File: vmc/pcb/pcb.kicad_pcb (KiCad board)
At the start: 2 copper layers, 85 x 90 mm, 88 parts, among them J1 Conn_02x08_Odd_Even, J10 ONE_WIRE_1, J11 ONE_WIRE_2, J12 AUX_1, J13 AUX_2, J14 AUX_3, J2 Conn_01x02_Pin, J3 24VAC, J4 MDB_CONN, J5 I2C header, J6 24VDC, J7 Conn_01x02, J8 Conn_01x02, J9 PICO_DEBUG_HEADER, Q1 BSS138, Q10 BSS138, Q11 BSS138, Q12 BSS138, Q13 BSS138, Q14 BC817, Q15 MMBT3906, Q16 BSS138, Q17 MMBT3906, Q2 BSS138, Q3 BSS138, Q4 BSS138, Q5 BSS138, Q6 BSS138, Q7 BSS138, Q8 BSS138, Q9 BSS138, U1 Pico, U2 74LS14

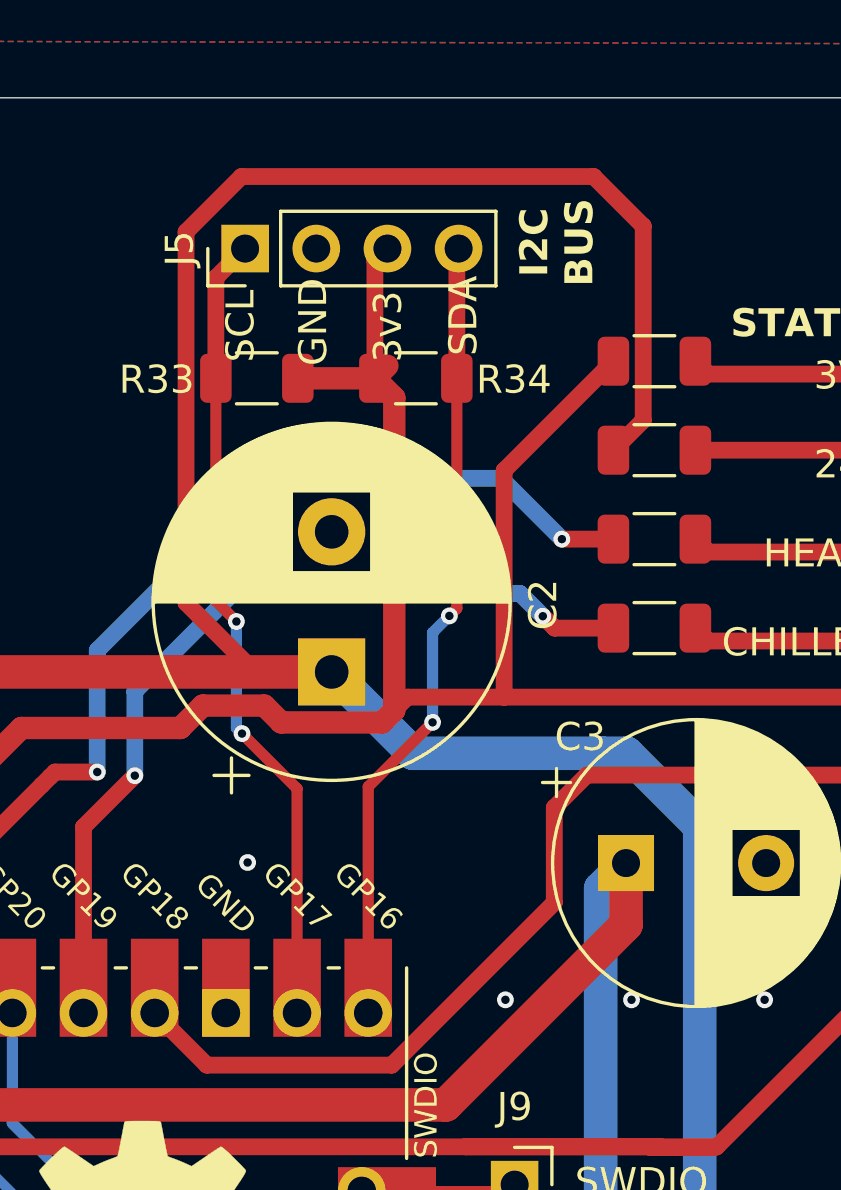
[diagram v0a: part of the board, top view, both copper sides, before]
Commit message: Updated PCB to thicken i2c data tracks and reroute the 24v led feed
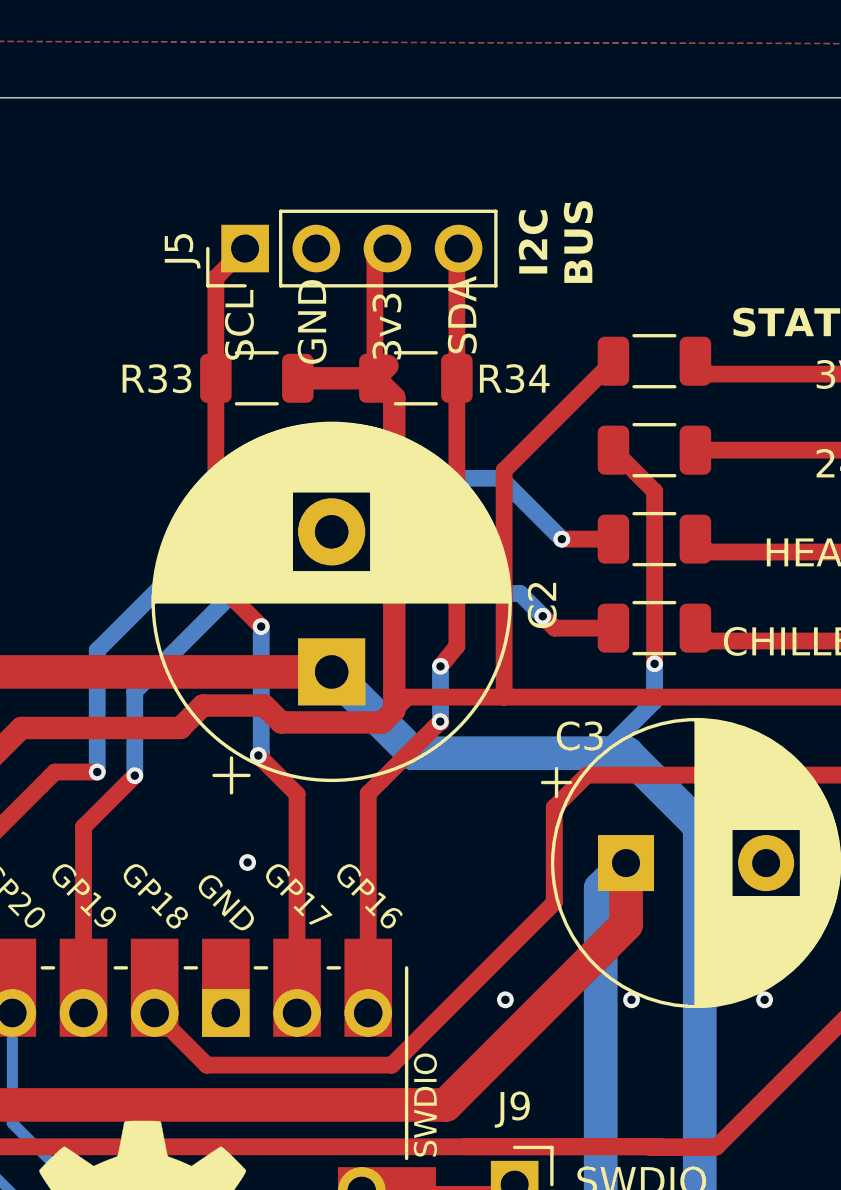
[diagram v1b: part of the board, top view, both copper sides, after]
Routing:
- net +24V: track 160.6 -> 127.0 mm, vias 0 -> 1
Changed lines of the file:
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@@
-	)
-	(segment
-		(start 60.773481 18)
-		(end 73.346502 18)
-		(width 0.6)
-		(layer "F.Cu")
-		(net 34)
-	)
-	(segment
-		(start 75.1135 19.766998)
-		(end 75.1135 26.7015)
-		(width 0.6)
-		(layer "F.Cu")
-		(net 34)
 	)
 	(segment
@@
 	)
 	(segment
-		(start 63.995481 35.678787)
-		(end 61.262695 35.678787)
-		(width 0.6)
-		(layer "F.Cu")
-		(net 34)
-	)
-	(segment
 		(start 46.878787 35.678787)
 		(end 46.84 35.64)
@@
 	)
 	(segment
-		(start 58.799 19.974481)
-		(end 60.773481 18)
+		(start 75.52 29.235)
+		(end 75.52 35.39)
 		(width 0.6)
 		(layer "F.Cu")
@@
 	)
 	(segment
-		(start 73.346502 18)
-		(end 75.1135 19.766998)
-		(width 0.6)
-		(layer "F.Cu")
-		(net 34)
-	)
-	(segment
-		(start 58.799 33.215092)
-		(end 58.799 19.974481)
-		(width 0.6)
-		(layer "F.Cu")
-		(net 34)
-	)
-	(segment
 		(start 63.935481 35.618787)
 		(end 63.995481 35.678787)
@@
 	)
 	(segment
-		(start 75.1135 26.7015)
-		(end 74.05 27.765)
-		(width 0.6)
-		(layer "F.Cu")
-		(net 34)
-	)
-	(segment
-		(start 61.262695 35.678787)
-		(end 58.799 33.215092)
+		(start 74.05 27.765)
+		(end 75.52 29.235)
 		(width 0.6)
 		(layer "F.Cu")
@@
 		(net 34)
 	)
+	(via
+		(at 75.52 35.39)
+		(size 0.6)
+		(drill 0.3)
+		(layers "F.Cu" "B.Cu")
+		(net 34)
+	)
 	(segment
 		(start 81.901531 74.651531)
@@
 	)
 	(segment
+		(start 75.52 36.719787)
+		(end 73.66 38.579787)
+		(width 0.6)
+		(layer "B.Cu")
+		(net 34)
+	)
+	(segment
 		(start 73.66 38.579787)
 		(end 66.896481 38.579787)
@@
 	)
 	(segment
+		(start 75.52 35.39)
+		(end 75.52 36.719787)
+		(width 0.6)
+		(layer "B.Cu")
+		(net 34)
+	)
+	(segment
 		(start 81.901531 90.157611)
 		(end 81.901531 74.651531)
@@
 	)
 	(segment
-		(start 60.595481 33.878787)
-		(end 59.8625 33.145806)
-		(width 0.4)
+		(start 62.76 40.04)
+		(end 61.38 38.66)
+		(width 0.6)
 		(layer "F.Cu")
 		(net 48)
@@
 	)
 	(segment
-		(start 59.8625 33.145806)
-		(end 59.8625 25.2)
-		(width 0.4)
-		(layer "F.Cu")
-		(net 48)
-	)
-	(segment
-		(start 62.76 39.843306)
-		(end 60.795481 37.878787)
-		(width 0.4)
+		(start 59.8625 25.2)
+		(end 59.8625 32.4425)
+		(width 0.6)
+		(layer "F.Cu")
+		(net 48)
+	)
+	(segment
+		(start 59.8625 32.4425)
+		(end 61.48 34.06)
+		(width 0.6)
 		(layer "F.Cu")
 		(net 48)
@@
 	(segment
 		(start 62.76 47.848787)
-		(end 62.76 39.843306)
-		(width 0.4)
+		(end 62.76 40.04)
+		(width 0.6)
 		(layer "F.Cu")
 		(net 48)
@@
 	)
 	(via
-		(at 60.595481 33.878787)
-		(size 0.6)
-		(drill 0.3)
-		(layers "F.Cu" "B.Cu")
-		(net 48)
-	)
-	(via
-		(at 60.795481 37.878787)
-		(size 0.6)
-		(drill 0.3)
-		(layers "F.Cu" "B.Cu")
-		(net 48)
-	)
-	(segment
-		(start 60.595481 33.878787)
-		(end 60.595481 37.678787)
-		(width 0.4)
-		(layer "B.Cu")
-		(net 48)
-	)
-	(segment
-		(start 60.595481 37.678787)
-		(end 60.795481 37.878787)
-		(width 0.4)
-		(layer "B.Cu")
-		(net 48)
-	)
-	(segment
-		(start 65.3 39.774268)
-		(end 67.595481 37.478787)
-		(width 0.4)
+		(at 61.48 34.06)
+		(size 0.6)
+		(drill 0.3)
+		(layers "F.Cu" "B.Cu")
+		(net 48)
+	)
+	(via
+		(at 61.38 38.66)
+		(size 0.6)
+		(drill 0.3)
+		(layers "F.Cu" "B.Cu")
+		(net 48)
+	)
+	(segment
+		(start 61.48 34.06)
+		(end 61.48 38.56)
+		(width 0.6)
+		(layer "B.Cu")
+		(net 48)
+	)
+	(segment
+		(start 61.48 38.56)
+		(end 61.38 38.66)
+		(width 0.6)
+		(layer "B.Cu")
+		(net 48)
+	)
+	(segment
+		(start 65.3 47.848787)
+		(end 65.3 40.02)
+		(width 0.6)
 		(layer "F.Cu")
 		(net 49)
@@
 	)
 	(segment
-		(start 68.195481 33.678787)
-		(end 68.4625 33.411768)
-		(width 0.4)
-		(layer "F.Cu")
-		(net 49)
-	)
-	(segment
-		(start 65.3 47.848787)
-		(end 65.3 39.774268)
-		(width 0.4)
+		(start 67.88 35.48)
+		(end 68.4625 34.7575)
+		(width 0.6)
+		(layer "F.Cu")
+		(net 49)
+	)
+	(segment
+		(start 65.3 40.02)
+		(end 65.78 39.54)
+		(width 0.6)
+		(layer "F.Cu")
+		(net 49)
+	)
+	(segment
+		(start 68.4625 34.7575)
+		(end 68.4625 25.2)
+		(width 0.6)
+		(layer "F.Cu")
+		(net 49)
+	)
+	(segment
+		(start 67.87 37.45)
+		(end 67.899787 37.479787)
+		(width 0.6)
+		(layer "F.Cu")
+		(net 49)
+	)
+	(segment
+		(start 65.78 39.54)
+		(end 67.87 37.45)
+		(width 0.6)
 		(layer "F.Cu")
 		(net 49)
@@
 		(net 49)
 	)
-	(segment
-		(start 68.4625 33.411768)
-		(end 68.4625 25.2)
-		(width 0.4)
-		(layer "F.Cu")
-		(net 49)
-	)
-	(via
-		(at 68.195481 33.678787)
-		(size 0.6)
-		(drill 0.3)
-		(layers "F.Cu" "B.Cu")
-		(net 49)
-	)
-	(via
-		(at 67.595481 37.478787)
-		(size 0.6)
-		(drill 0.3)
-		(layers "F.Cu" "B.Cu")
-		(net 49)
-	)
-	(segment
-		(start 67.595481 37.478787)
-		(end 67.595481 34.278787)
-		(width 0.4)
-		(layer "B.Cu")
-		(net 49)
-	)
-	(segment
-		(start 67.595481 34.278787)
-		(end 68.195481 33.678787)
-		(width 0.4)
-		(layer "B.Cu")
-		(net 49)
+	(via
+		(at 67.88 35.48)
+		(size 0.6)
+		(drill 0.3)
+		(layers "F.Cu" "B.Cu")
+		(net 49)
+	)
+	(via
+		(at 67.87 37.45)
+		(size 0.6)
+		(drill 0.3)
+		(layers "F.Cu" "B.Cu")
+		(net 49)
+	)
+	(segment
+		(start 67.88 37.44)
+		(end 67.87 37.45)
+		(width 0.6)
+		(layer "B.Cu")
+		(net 49)
+	)
+	(segment
+		(start 67.88 35.48)
+		(end 67.88 37.44)
+		(width 0.6)
+		(layer "B.Cu")
+		(net 49)

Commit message: Fix missing ground connection on shift register IC (ground plane continuity failure)
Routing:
- net GND: vias 30 -> 45
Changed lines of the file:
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@@
+	)
+	(via
+		(at 30.09 97.02)
+		(size 0.6)
+		(drill 0.3)
+		(layers "F.Cu" "B.Cu")
+		(free yes)
+		(net 16)
 	)
 	(via
@@
 	)
 	(via
+		(at 53.02 94.29)
+		(size 0.6)
+		(drill 0.3)
+		(layers "F.Cu" "B.Cu")
+		(free yes)
+		(net 16)
+	)
+	(via
 		(at 79.445481 57.628787)
 		(size 0.6)
@@
 	)
 	(via
+		(at 85.98 69.77)
+		(size 0.6)
+		(drill 0.3)
+		(layers "F.Cu" "B.Cu")
+		(free yes)
+		(net 16)
+	)
+	(via
 		(at 60.995481 42.478787)
 		(size 0.6)
@@
 	)
 	(via
+		(at 53.52 30.11)
+		(size 0.6)
+		(drill 0.3)
+		(layers "F.Cu" "B.Cu")
+		(free yes)
+		(net 16)
+	)
+	(via
+		(at 79.34 60.81)
+		(size 0.6)
+		(drill 0.3)
+		(layers "F.Cu" "B.Cu")
+		(free yes)
+		(net 16)
+	)
+	(via
 		(at 74.695481 47.378787)
 		(size 0.6)
@@
 	)
 	(via
+		(at 75.34 69.68)
+		(size 0.6)
+		(drill 0.3)
+		(layers "F.Cu" "B.Cu")
+		(free yes)
+		(net 16)
+	)
+	(via
 		(at 32.195481 57.878787)
 		(size 0.6)
@@
 	)
 	(via
+		(at 70.52 63.25)
+		(size 0.6)
+		(drill 0.3)
+		(layers "F.Cu" "B.Cu")
+		(free yes)
+		(net 16)
+	)
+	(via
 		(at 70.445481 87.878787)
 		(size 0.6)
@@
 	)
 	(via
+		(at 81.51 69.77)
+		(size 0.6)
+		(drill 0.3)
+		(layers "F.Cu" "B.Cu")
+		(free yes)
+		(net 16)
+	)
+	(via
+		(at 30.03 94.96)
+		(size 0.6)
+		(drill 0.3)
+		(layers "F.Cu" "B.Cu")
+		(free yes)
+		(net 16)
+	)
+	(via
 		(at 22.795481 43.878787)
 		(size 0.6)
@@
 	)
 	(via
+		(at 28.15 95.02)
+		(size 0.6)
+		(drill 0.3)
+		(layers "F.Cu" "B.Cu")
+		(free yes)
+		(net 16)
+	)
+	(via
 		(at 63.695481 54.878787)
 		(size 0.6)
@@
 	)
 	(via
+		(at 53.61 19.63)
+		(size 0.6)
+		(drill 0.3)
+		(layers "F.Cu" "B.Cu")
+		(free yes)
+		(net 16)
+	)
+	(via
 		(at 83.84 82.82)
 		(size 0.6)
@@
 	)
 	(via
+		(at 79.42 64.3)
+		(size 0.6)
+		(drill 0.3)
+		(layers "F.Cu" "B.Cu")
+		(free yes)
+		(net 16)
+	)
+	(via
 		(at 48.195481 43.678787)
 		(size 0.6)
@@
 	)
 	(via
+		(at 53.61 24.5)
+		(size 0.6)
+		(drill 0.3)
+		(layers "F.Cu" "B.Cu")
+		(free yes)
+		(net 16)
+	)
+	(via
 		(at 77.595481 79.678787)
 		(size 0.6)
@@
 		(size 0.6)
 		(drill 0.3)
+		(layers "F.Cu" "B.Cu")
+		(free yes)
+		(net 16)
+	)
+	(via
+		(at 75.06 74.4)
+		(size 0.6)
+		(drill 0.3)
+		(layers "F.Cu" "B.Cu")
+		(free yes)
+		(net 16)
+	)
+	(via
+		(at 73.72 77.71)
+		(size 0.6)
+		(drill 0.3)

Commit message: More layout tweaks
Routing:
- net +5V: track 317.7 -> 298.6 mm
- net +24V: track 127.0 -> 130.9 mm
- net +3V3: track 470.0 -> 468.8 mm

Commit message: Add resistor values
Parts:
- R37: value 700R -> 750R
- R38: value R -> 1.4K
- R39, R40, R41: value R -> 5.1R
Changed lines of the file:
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@@
 			)
 		)
-		(property "Value" "R"
+		(property "Value" "5.1R"
 			(at 0 1.82 0)
 			(layer "F.Fab")
@@
 			)
 		)
-		(property "Value" "700R"
+		(property "Value" "750R"
 			(at 0 1.82 90)
 			(layer "F.Fab")
@@
 			)
 		)
-		(property "Value" "R"
+		(property "Value" "5.1R"
 			(at -5.465 -0.085 0)
 			(layer "F.Fab")
@@
 			)
 		)
-		(property "Value" "R"
+		(property "Value" "5.1R"
 			(at 0 1.82 0)
 			(layer "F.Fab")
@@
 			)
 		)
-		(property "Value" "R"
+		(property "Value" "1.4K"
 			(at -0.25 -1.355 0)
 			(layer "F.Fab")

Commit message: Add version number to PCB (v1.1) Whitespace formatting
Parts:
- moved REF** 23.2 mm to (77.5, 68.5)
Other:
- board text added: "V 1.1"
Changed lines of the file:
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@@
 	(footprint "Symbol:OSHW-Logo2_14.6x12mm_SilkScreen"
 		(layer "F.Cu")
-		(at 57.25 57.25)
+		(at 77.5 68.5)
 		(descr "Open Source Hardware Symbol")
 		(tags "Logo Symbol OSHW")
@@
 	)
 	(gr_text "Snackbot Motor Driver/MDB interface\nwww.github.com/davidmpye/snackbot"
-		(at 35 63.25 0)
+		(at 46.5 42 0)
 		(layer "F.SilkS")
 		(effects
@@
 		)
 	)
+	(gr_text "V 1.1"
+		(at 63.5 42 0)
+		(layer "F.SilkS")
+		(effects
+			(font
+				(size 1.5 1.5)
+				(thickness 0.3)
+				(bold yes)
+			)
+			(justify left bottom)
+		)
+	)
 	(gr_text "3V3"
 		(at 81.2 25.685 0)
@@
 	)
 	(gr_text "Pico Here"
-		(at 26.5 56.5 0)
+		(at 32.5 58.5 0)
 		(layer "F.SilkS")
 		(effects
